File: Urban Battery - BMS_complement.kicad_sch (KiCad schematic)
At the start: 37 parts, among them J1 BMS IO, J10 Thermistor, J11 Thermistor, J12 CAN Connector, J13 CAN Connector, J2 OLED Header, J3 E-Stop, J4 E-Stop, J5 E-Stop, J6 Contactor Connector, J7 Charge Connector, J8 Battery Connector, J9 Thermistor, K1 Contactor_Relay, K2 Charge_Relay, SW1 SW_Push_LED, SW2 SW_DPDT_x2, SW3 CAN_TERM, U1 MCP2515-xSO, U2 LM2575HVS-12/NOPB, U3 MCP2551-I-SN, Y1 8MHz

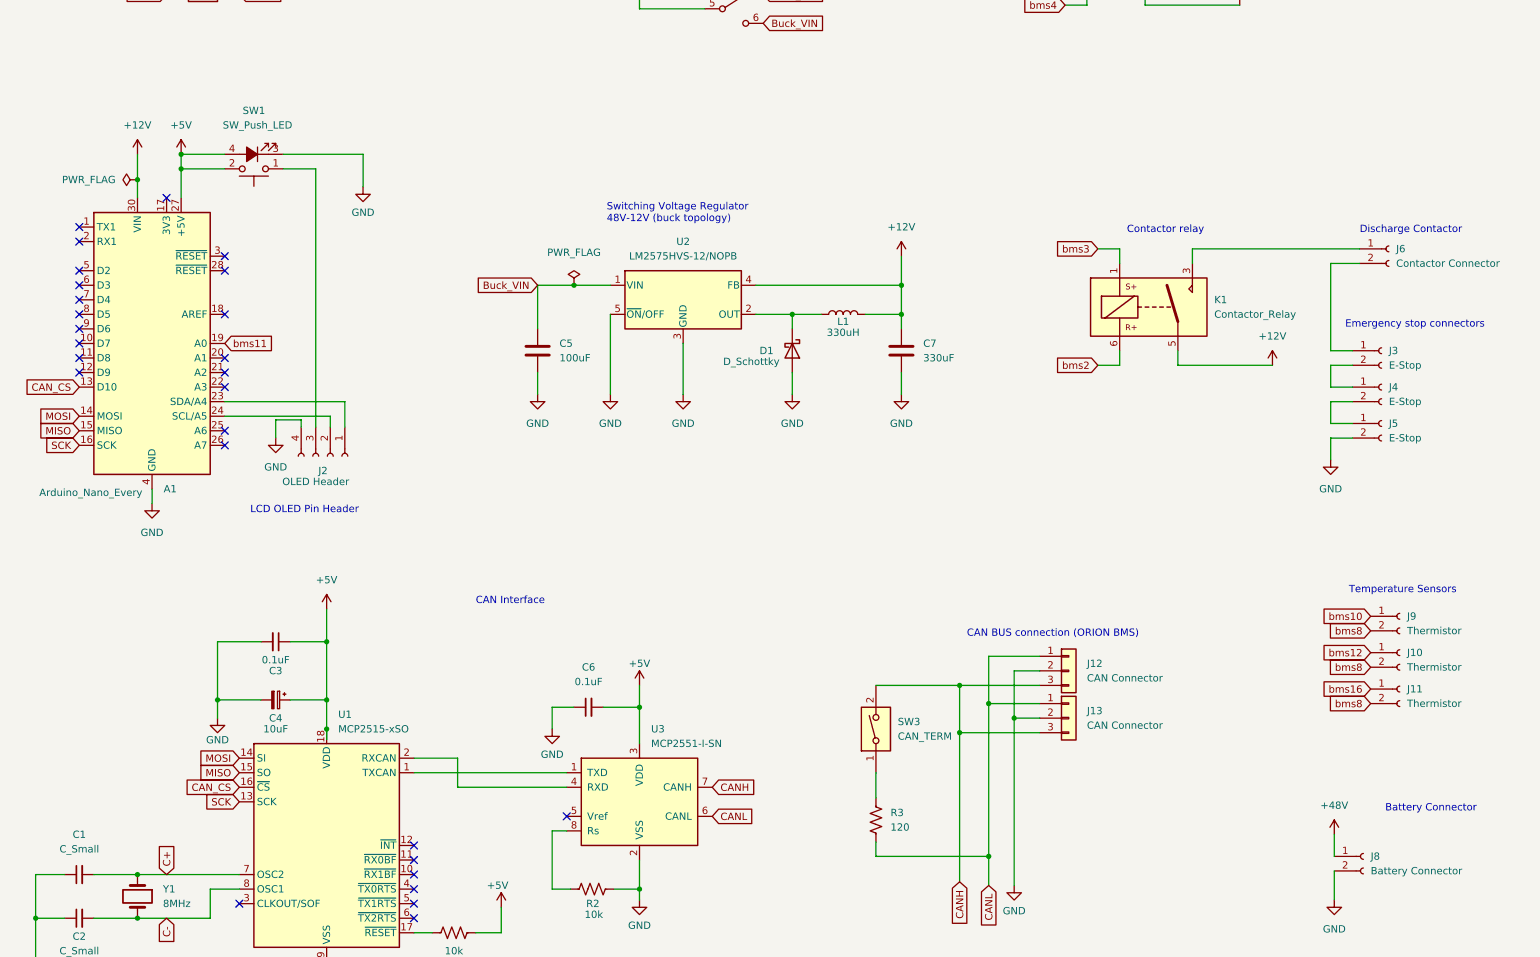
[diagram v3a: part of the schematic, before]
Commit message: added can_int, changed oled button, added 4th safety switch
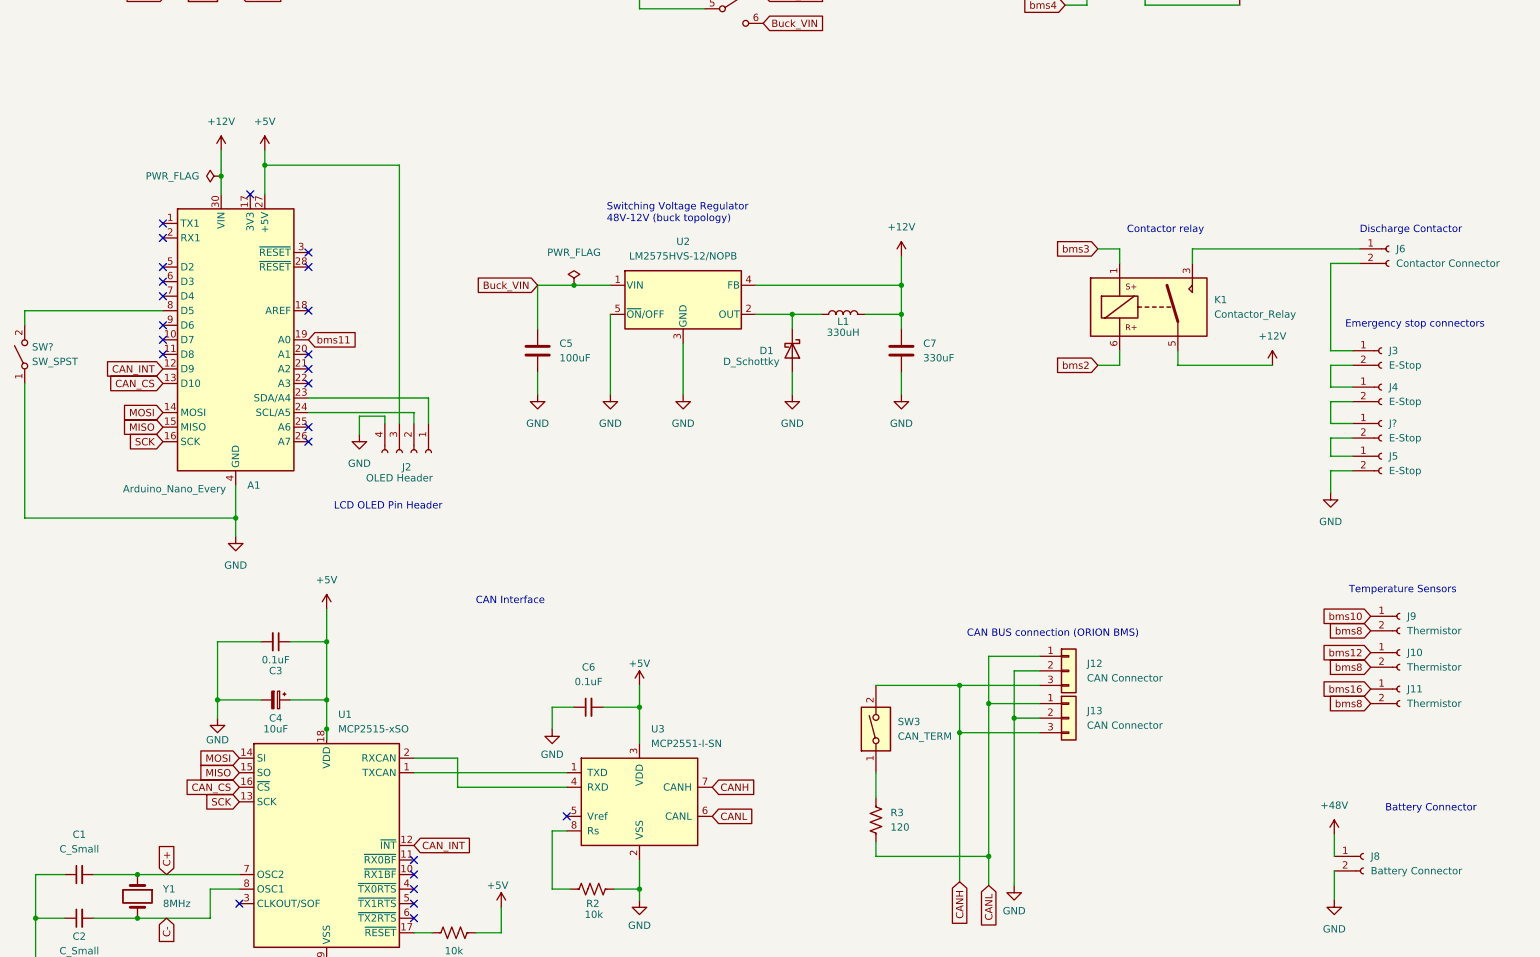
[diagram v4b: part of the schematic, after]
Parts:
- removed SW1: SW_Push_LED, Button_Switch_THT:SW_Push_1P1T_NO_LED_E-Switch_TL1250, symbol Switch:SW_Push_LED
- added J?: E-Stop, Connector_Molex:Molex_Micro-Fit_3.0_43650-0200_1x02_P3.00mm_Horizontal, symbol Connector:Conn_01x02_Female
- added SW?: SW_SPST, symbol Switch:SW_SPST
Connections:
- net +5V: now also J2.3 (Pin_3)
- net GND: now also SW?.1 (A)
- net at J4.2 (Pin_2): now also J?.1 (Pin_1); no longer J5.1 (Pin_1)
- net CAN_INT: now reaches A1.12 (D9)
- net CAN_INT: now also U1.12 (~{INT})
- net at A1.8 (D5): now also SW?.2 (B)
- new net: J5.1 (Pin_1), J?.2 (Pin_2)
- no-connect marks 35 -> 32
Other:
- moved on the sheet: A1, J2, J5

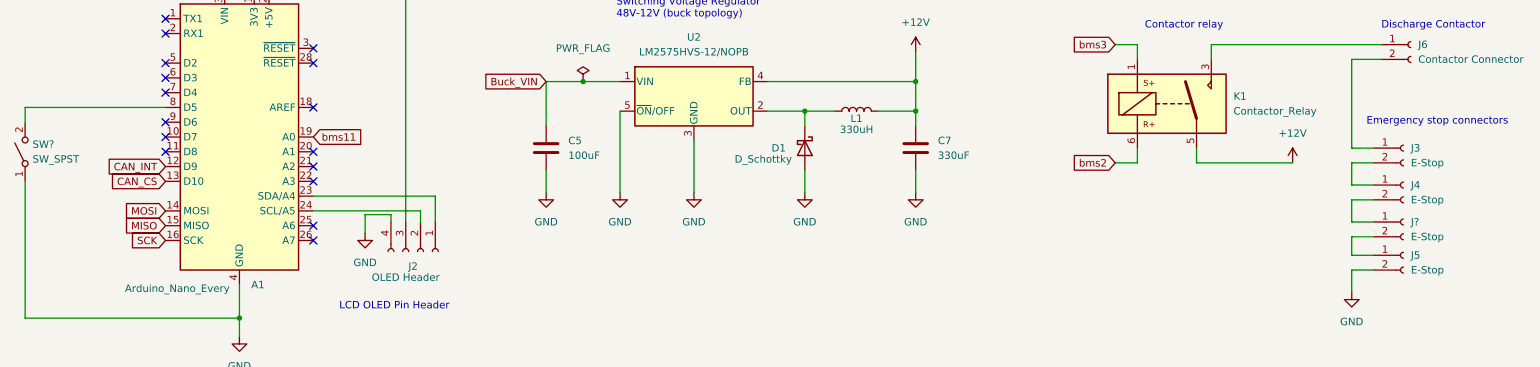
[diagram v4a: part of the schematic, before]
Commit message: updated layout from schematic, deleted traces
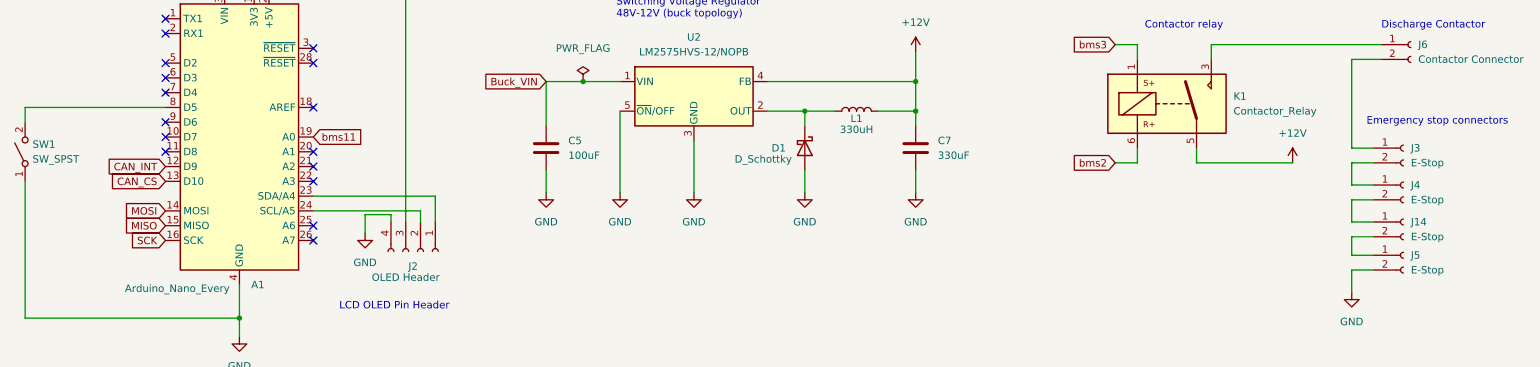
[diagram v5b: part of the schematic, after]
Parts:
- SW1: renamed from SW?; footprint (none) -> Button_Switch_THT:SW_Tactile_SPST_Angled_PTS645Vx31-2LFS
- gave numbers to parts that had none: 1
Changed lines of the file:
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@@
   (symbol (lib_id "Switch:SW_SPST") (at 23.495 139.065 90) (unit 1)
     (in_bom yes) (on_board yes) (fields_autoplaced)
-    (property "Reference" "SW?" (id 0) (at 24.765 137.7949 90)
+    (property "Reference" "SW1" (id 0) (at 24.765 137.7949 90)
       (effects (font (size 1.27 1.27)) (justify right))
     )
@@
       (effects (font (size 1.27 1.27)) (justify right))
     )
-    (property "Footprint" "" (id 2) (at 23.495 139.065 0)
+    (property "Footprint" "Button_Switch_THT:SW_Tactile_SPST_Angled_PTS645Vx31-2LFS" (id 2) (at 23.495 139.065 0)
       (effects (font (size 1.27 1.27)) hide)
     )
@@
   (symbol (lib_id "Connector:Conn_01x02_Female") (at 260.35 151.13 0) (unit 1)
     (in_bom yes) (on_board yes) (fields_autoplaced)
-    (property "Reference" "J?" (id 0) (at 261.62 151.1299 0)
+    (property "Reference" "J14" (id 0) (at 261.62 151.1299 0)
       (effects (font (size 1.27 1.27)) (justify left))
     )
@@
     )
     (path "/ab956923-6b68-4281-8489-3a05b7f8dae5"
-      (reference "J?") (unit 1) (value "E-Stop") (footprint "Connector_Molex:Molex_Micro-Fit_3.0_43650-0200_1x02_P3.00mm_Horizontal")
+      (reference "J14") (unit 1) (value "E-Stop") (footprint "Connector_Molex:Molex_Micro-Fit_3.0_43650-0200_1x02_P3.00mm_Horizontal")
     )
     (path "/ea90f9ac-3a1c-4bd6-87e3-9c84b8c1984a"
@@
       (reference "R3") (unit 1) (value "120") (footprint "Resistor_SMD:R_0805_2012Metric_Pad1.20x1.40mm_HandSolder")
     )
+    (path "/5dea82e6-e5a0-4de1-8cf9-6e3092f66205"
+      (reference "SW1") (unit 1) (value "SW_SPST") (footprint "Button_Switch_THT:SW_Tactile_SPST_Angled_PTS645Vx31-2LFS")
+    )
     (path "/3e1e1fe7-4a2f-4d8a-9ee6-adb86443cfc4"
       (reference "SW2") (unit 1) (value "SW_DPDT_x2") (footprint "BMS_Custom_Footprints:Toggle_Switch_M2022S2A2W30")
@@
       (reference "SW3") (unit 1) (value "CAN_TERM") (footprint "Connector_PinHeader_2.54mm:PinHeader_1x02_P2.54mm_Vertical")
     )
-    (path "/5dea82e6-e5a0-4de1-8cf9-6e3092f66205"
-      (reference "SW?") (unit 1) (value "SW_SPST") (footprint "")
-    )
     (path "/38a517b7-e3ff-44bb-944f-e8a6ce592fe9"

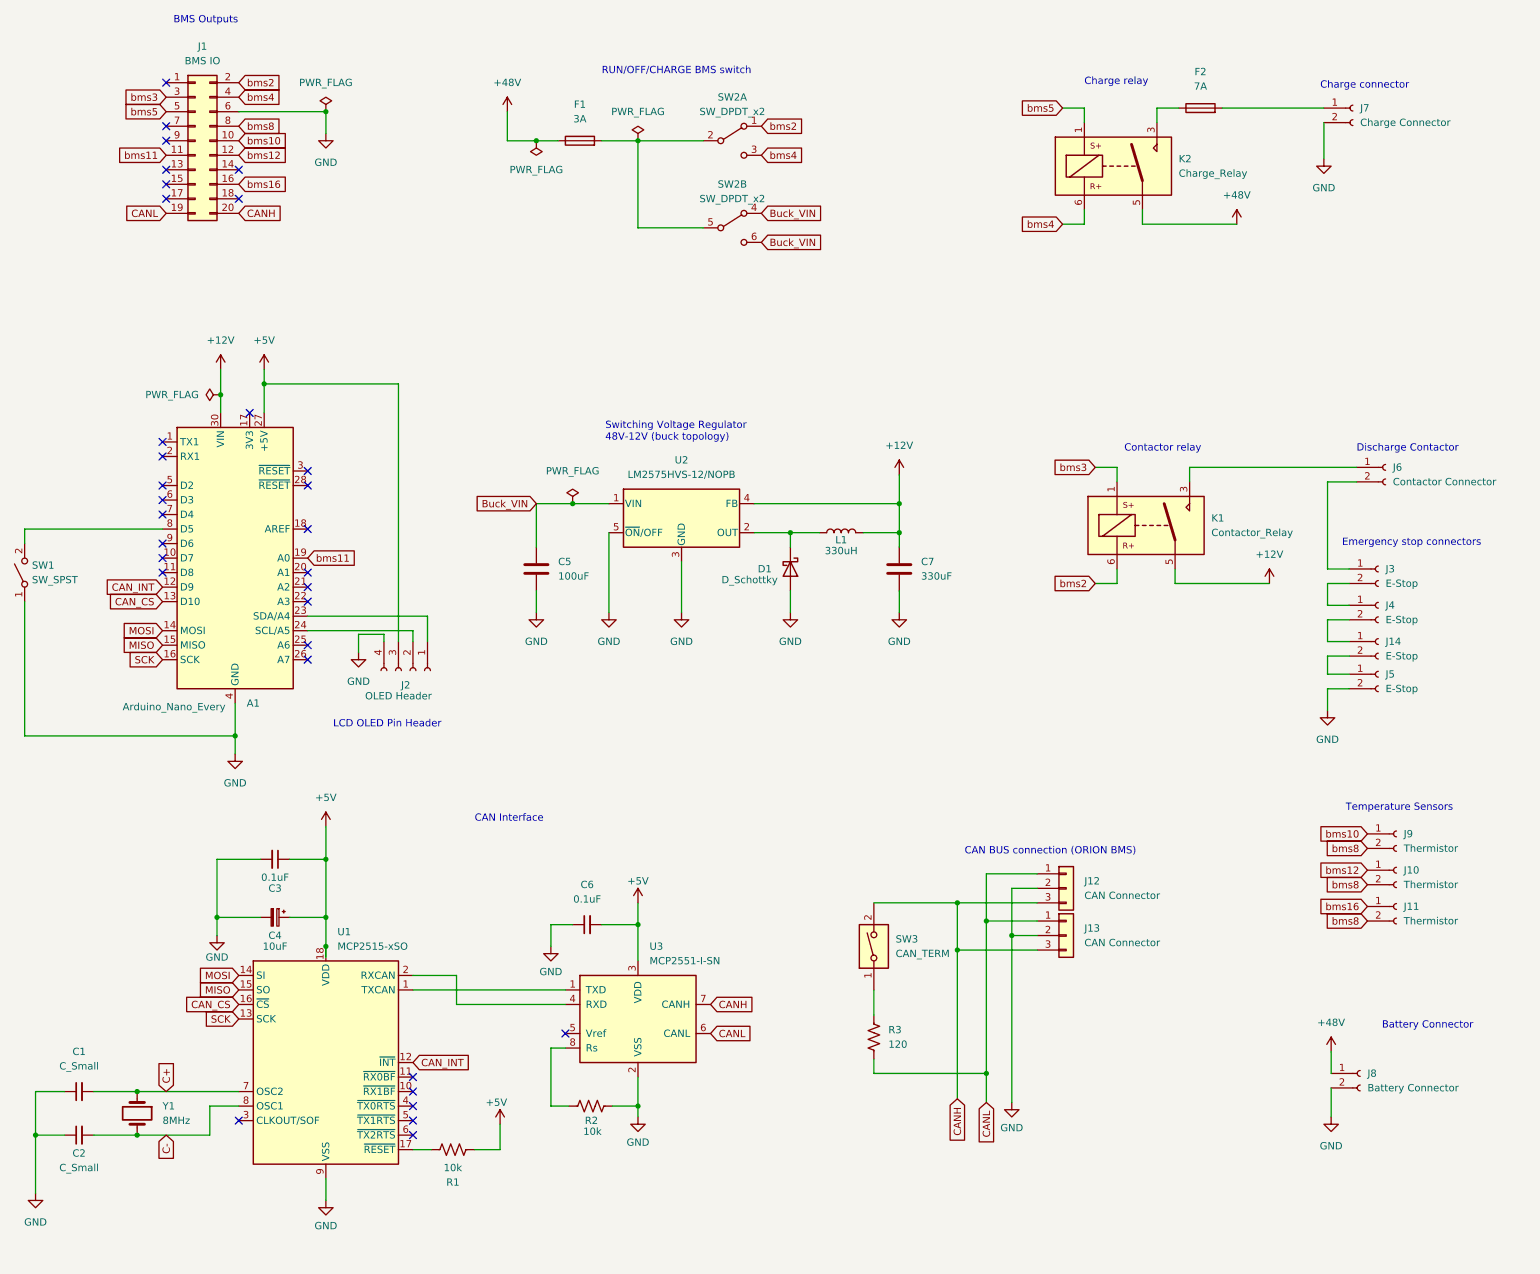
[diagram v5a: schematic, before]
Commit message: First layout complete
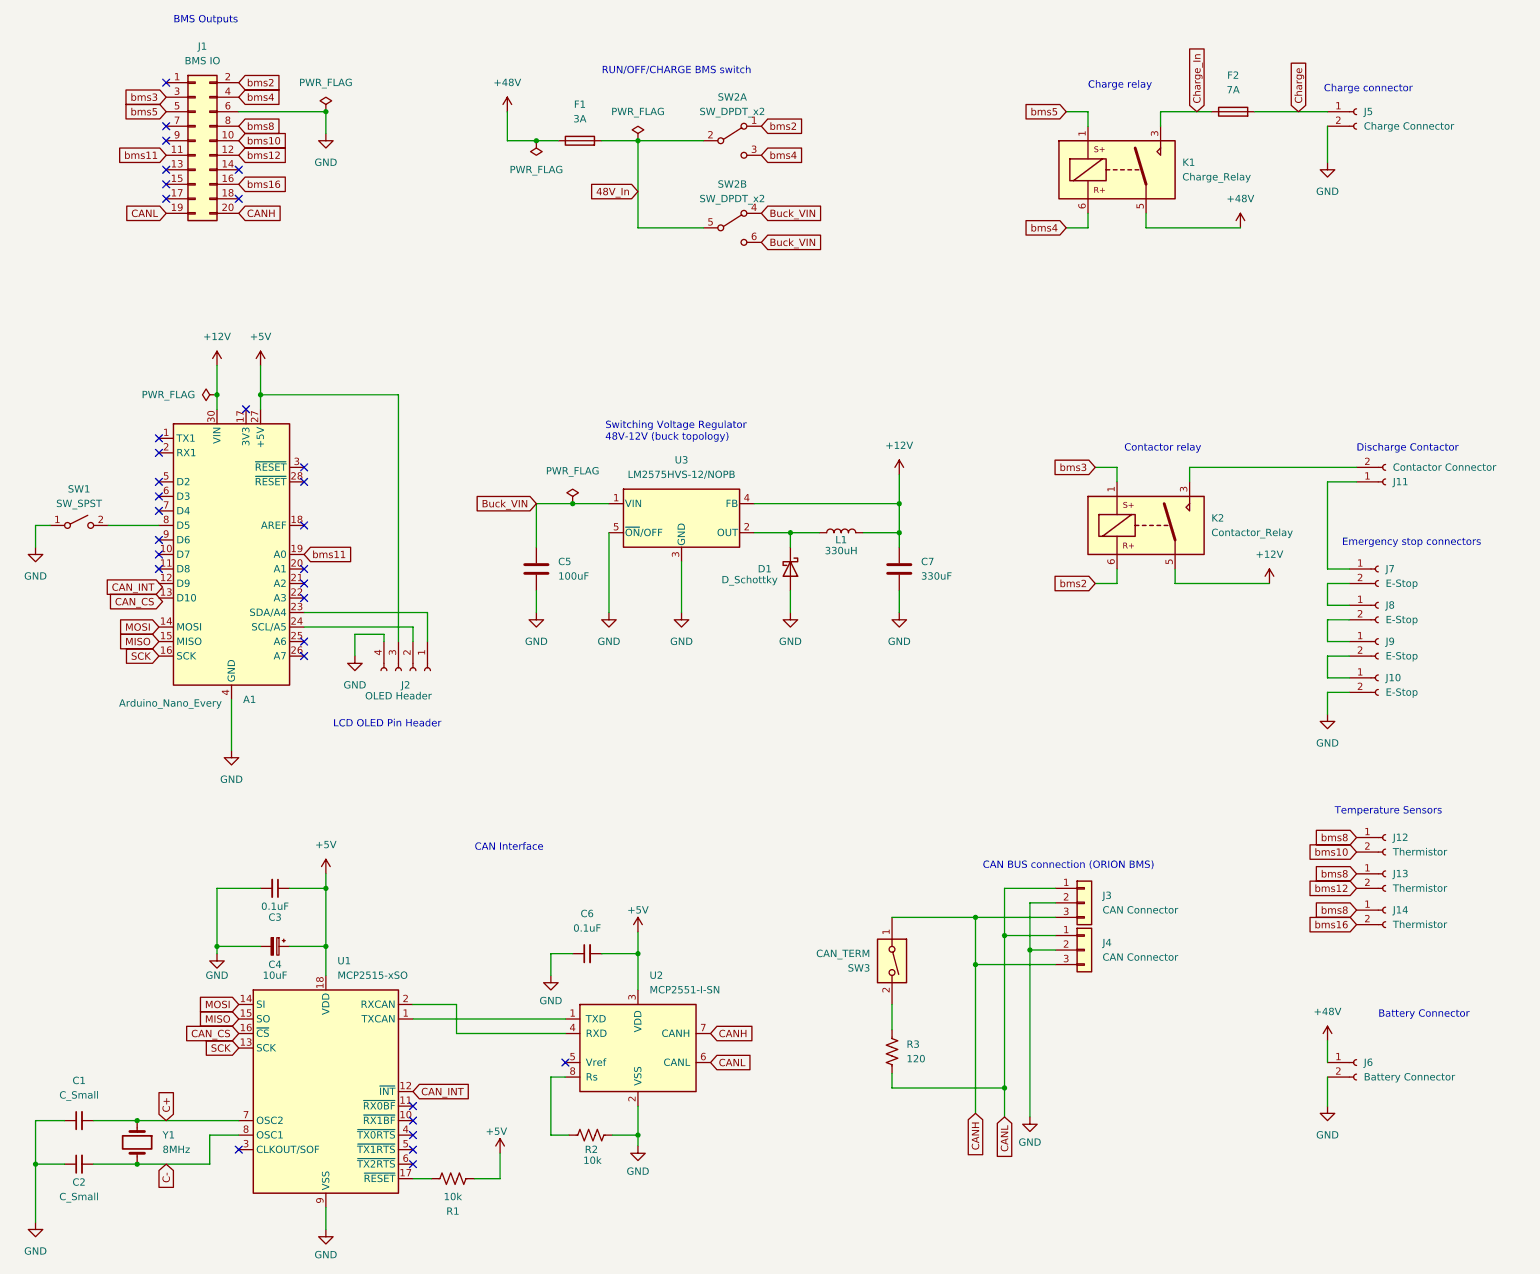
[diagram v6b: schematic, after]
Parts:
- SW3: footprint Connector_PinHeader_2.54mm:PinHeader_1x02_P2.54mm_Vertical -> Connector_PinHeader_2.54mm:PinHeader_1x02_P2.54mm_Horizontal
- renumbered J5 to J10, J6 to J11, J9 to J12, J10 to J13, J11 to J14, J12 to J3, J13 to J4, J7 to J5, J8 to J6, J3 to J7, J4 to J8, J14 to J9, K2 to K1, K1 to K2, U3 to U2, U2 to U3
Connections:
- net CANH: now also SW3.1; no longer SW3.2
- net CAN_CS: no longer A1.13 (D10)
- net CAN_INT: no longer A1.12 (D9)
- net bms10: now also J12.2 (Pin_2); no longer J12.1 (Pin_1)
- net bms12: now also J13.2 (Pin_2); no longer J13.1 (Pin_1)
- net bms16: now also J14.2 (Pin_2); no longer J14.1 (Pin_1)
- net bms8: now also J12.1 (Pin_1), J13.1 (Pin_1), J14.1 (Pin_1); no longer J12.2 (Pin_2), J13.2 (Pin_2), J14.2 (Pin_2)
- net at R3.1: now also SW3.2; no longer SW3.1
- net 48V_In: now reaches F1.2, SW2.2 (B), SW2.5 (B)
- net Charge_In: now reaches F2.1, K1.3
- net Charge: now reaches F2.2, J5.1 (Pin_1)
- net at J11.1 (Pin_1): now also J7.1 (Pin_1); no longer K2.3
- net at J11.2 (Pin_2): now also K2.3; no longer J7.1 (Pin_1)
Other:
- moved on the sheet: A1, C1, C2, C3, C4, C6, F2, J10, J12, J13, J14, J3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

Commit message: Layout updated
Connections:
- net bms11: now also A1.22 (A3); no longer A1.19 (A0)
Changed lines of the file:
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@@
   (no_connect (at 72.39 138.43))
   (no_connect (at 72.39 140.97))
-  (no_connect (at 72.39 143.51))
   (no_connect (at 72.39 151.13))
   (no_connect (at 72.39 153.67))
@@
   (no_connect (at 72.39 120.65))
   (no_connect (at 72.39 123.19))
+  (no_connect (at 72.39 135.89))
   (no_connect (at 48.26 63.5))
   (no_connect (at 48.26 60.96))
@@
     )
   )
-  (global_label "bms11" (shape input) (at 72.39 135.89 0) (fields_autoplaced)
-    (effects (font (size 1.27 1.27)) (justify left))
-    (property "Intersheet References" "${INTERSHEET_REFS}" (id 0) (at 81.0926 135.8106 0)
-      (effects (font (size 1.27 1.27)) (justify left) hide)
-    )
+  (global_label "bms11" (shape input) (at 72.39 143.51 0) (fields_autoplaced)
+    (effects (font (size 1.27 1.27)) (justify left))
+    (property "Intersheet References" "${INTERSHEET_REFS}" (id 0) (at 81.0926 143.4306 0)
+      (effects (font (size 1.27 1.27)) (justify left) hide)
+    )
